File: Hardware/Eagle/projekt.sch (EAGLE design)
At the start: 140 parts, among them IC1 MEGA16-P, IC2 7805T, Q1 BC807-40SMD, Q10 2N2222, Q11 2N2222, Q12 2N2222, Q13 BC807-40SMD, Q14 BC807-40SMD, Q15 BC807-40SMD, Q16 BC807-40SMD, Q17 BC807-40SMD, Q18 BC807-40SMD, Q19 BC807-40SMD, Q2 BC807-40SMD, Q20 2N2222, Q22 2N2222, Q24 2N2222, Q26 2N2222, Q27 2N2222, Q29 2N2222, Q3 BC807-40SMD, Q30 2N2222, Q4 BC807-40SMD, Q5 BC807-40SMD, Q6 2N2222, Q7 2N2222, Q8 2N2222, Q9 2N2222

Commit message: generalne porzadki w kodzie i schemacie
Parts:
- removed LED1, LED2, LED3, LED4, LED5: LA-401AD, led-7-segment:LA-401AD
- added D1, D2, D3, D4, D5: (no value), special:7SEG-CA
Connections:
- net ZASILACZ_1 renamed POWER_1
- net ZASILACZ_2 renamed POWER_2
- removed net N$28: IC1.(TMS)PC3, R1.1
- removed net N$30: IC1.(OC1A)PD5, R14.1
- removed net N$31: IC1.(RXD)PD0, R19.1
- removed net N$32: IC1.(TXD)PD1, R18.1
- removed net N$33: IC1.(INT0)PD2, R17.1
- removed net N$34: IC1.(INT1)PD3, R16.1
- removed net N$35: IC1.(OC1B)PD4, R15.1
- removed net N$37: IC1.(ICP)PD6, R13.1
- removed net N$44: IC1.(OC2)PD7, R5.1
- removed net N$46: IC1.(SCL)PC0, R4.1
- removed net N$47: IC1.(SDA)PC1, R3.1
- removed net N$49: IC1.(TCK)PC2, R2.1
- removed net N$50: IC1.(TDO)PC4, R27.1
- removed net N$64: IC1.(TDI)PC5, R28.1
- removed net N$67: IC1.(TOSC1)PC6, R29.1
- removed net N$68: IC1.(TOSC2)PC7, R30.1
- removed net N$69: IC1.(T0/XCK)PB0, R31.1
- removed net N$7: LED1.G, LED2.G, LED3.G, LED4.G, LED5.G, R12.2
- removed net N$70: IC1.(T1)PB1, R32.1
- removed net N$71: IC1.(ADC0)PA0, R33.1
- removed net N$72: IC1.(ADC1)PA1, R34.1
- removed net N$73: IC1.(ADC2)PA2, R35.1
- removed net N$74: IC1.(ADC3)PA3, R36.1
- removed net N$75: IC1.(ADC4)PA4, R38.1
- removed net N$76: IC1.(ADC5)PA5, R37.1
- removed net N$77: IC1.(ADC6)PA6, R39.1
- removed net N$98: IC1.(ADC7)PA7, R40.1
- new net DISP_ANO_0: IC1.(T0/XCK)PB0, R5.1
- new net DISP_ANO_1: IC1.(T1)PB1, R4.1
- new net DISP_ANO_2: IC1.(AIN0/INT2)PB2, R3.1
- new net DISP_ANO_3: IC1.(AIN1/OC0)PB3, R2.1
- new net DISP_ANO_4: IC1.(SS)PB4, R1.1
- new net DISP_SEG_A: IC1.(ADC0)PA0, R13.1
- new net DISP_SEG_B: IC1.(ADC1)PA1, R14.1
- new net DISP_SEG_C: IC1.(ADC2)PA2, R15.1
- new net DISP_SEG_D: IC1.(ADC3)PA3, R16.1
- new net DISP_SEG_E: IC1.(ADC4)PA4, R17.1
- new net DISP_SEG_F: IC1.(ADC5)PA5, R18.1
- new net DISP_SEG_G: IC1.(ADC6)PA6, R19.1
- new net LED_ANO_1: R40.1
- new net LED_ANO_2: R39.1
- new net LED_ANO_3: R37.1
- new net LED_ANO_4: R38.1
- new net LED_ANO_5: R36.1
- new net LED_ANO_6: R35.1
- new net LED_ANO_7: R34.1
- new net LED_CAT_1: R33.1
- new net LED_CAT_2: R32.1
- new net LED_CAT_3: R31.1
- new net LED_CAT_4: R30.1
- new net LED_CAT_5: R29.1
- new net LED_CAT_6: R28.1
- new net LED_CAT_7: R27.1
- new net N$25: D1.G, D2.G, D3.G, D4.G, D5.G, R12.2
- net KLAW_1: no longer IC1.(SCK)PB7
- net KLAW_2: no longer IC1.(MISO)PB6
- net KLAW_3: no longer IC1.(MOSI)PB5
- net KLAW_4: no longer IC1.(SS)PB4
- net KLAW_5: no longer IC1.(AIN1/OC0)PB3
- net KLAW_6: no longer IC1.(AIN0/INT2)PB2
- net N$1: now also D1.A, D2.A, D3.A, D4.A, D5.A; no longer LED1.A, LED2.A, LED3.A, LED4.A, LED5.A
- net N$10: now also D3.CA1, D3.CA2; no longer LED3.A@1, LED3.A@2
- net N$11: now also D4.CA1, D4.CA2; no longer LED4.A@1, LED4.A@2
- net N$12: now also D5.CA1, D5.CA2; no longer LED5.A@1, LED5.A@2
- net N$2: now also D1.B, D2.B, D3.B, D4.B, D5.B; no longer LED1.B, LED2.B, LED3.B, LED4.B, LED5.B
- net N$3: now also D1.C, D2.C, D3.C, D4.C, D5.C; no longer LED1.C, LED2.C, LED3.C, LED4.C, LED5.C
- net N$4: now also D1.D, D2.D, D3.D, D4.D, D5.D; no longer LED1.D, LED2.D, LED3.D, LED4.D, LED5.D
- net N$5: now also D1.E, D2.E, D3.E, D4.E, D5.E; no longer LED1.E, LED2.E, LED3.E, LED4.E, LED5.E
- net N$6: now also D1.F, D2.F, D3.F, D4.F, D5.F; no longer LED1.F, LED2.F, LED3.F, LED4.F, LED5.F
- net N$8: now also D1.CA1, D1.CA2; no longer LED1.A@1, LED1.A@2
- net N$9: now also D2.CA1, D2.CA2; no longer LED2.A@1, LED2.A@2
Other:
- note added: "330R"
- note added: "47u"
- note added: "7 SEGMENT DISPLAY"
- note added: "KEYBOARD"
- note added: "LED MATRIX"
- note added: "POWER SUPPLY"
- note added: "PROCESSOR"
- note removed: "???"
- note removed: "KLAWIATURA"
- note removed: "ZASILANIE"
- moved on the sheet: B1, C1, C2, C3, C4, C5, C6, C7, IC1, IC2, LED10, LED11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

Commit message: diody i klawiatura
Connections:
- removed net KLAW_1: S1.0@A, S1.0@B, S2.0@A, S2.0@B, S3.0@A, S3.0@B
- removed net KLAW_2: S4.0@A, S4.0@B, S5.0@A, S5.0@B, S6.0@A, S6.0@B
- removed net KLAW_3: S7.0@A, S7.0@B, S8.0@A, S8.0@B, S9.0@A, S9.0@B
- removed net KLAW_4: S3.1@A, S3.1@B, S4.1@A, S4.1@B, S9.1@A, S9.1@B
- removed net KLAW_5: S2.1@A, S2.1@B, S5.1@A, S5.1@B, S8.1@A, S8.1@B
- removed net KLAW_6: S1.1@A, S1.1@B, S6.1@A, S6.1@B, S7.1@A, S7.1@B
- removed net LED_ANO_7: R34.1
- new net KEY_1: IC1.(TOSC2)PC7, S1.0@A, S1.0@B, S2.0@A, S2.0@B, S3.0@A, S3.0@B
- new net KEY_2: IC1.(TOSC1)PC6, S4.0@A, S4.0@B, S5.0@A, S5.0@B, S6.0@A, S6.0@B
- new net KEY_3: IC1.(TDI)PC5, S7.0@A, S7.0@B, S8.0@A, S8.0@B, S9.0@A, S9.0@B
- new net KEY_4: IC1.(TDO)PC4, S3.1@A, S3.1@B, S4.1@A, S4.1@B, S9.1@A, S9.1@B
- new net KEY_5: IC1.(TMS)PC3, S2.1@A, S2.1@B, S5.1@A, S5.1@B, S8.1@A, S8.1@B
- new net KEY_6: IC1.(TCK)PC2, S1.1@A, S1.1@B, S6.1@A, S6.1@B, S7.1@A, S7.1@B
- new net LED_ANO_0: IC1.(ADC7)PA7, R40.1
- net LED_ANO_1: now also IC1.(SCK)PB7, R39.1; no longer R40.1
- net LED_ANO_2: now also IC1.(MISO)PB6, R37.1; no longer R39.1
- net LED_ANO_3: now also IC1.(MOSI)PB5, R38.1; no longer R37.1
- net LED_ANO_4: now also IC1.(SDA)PC1, R36.1; no longer R38.1
- net LED_ANO_5: now also IC1.(SCL)PC0, R35.1; no longer R36.1
- net LED_ANO_6: now also IC1.(OC2)PD7, R34.1; no longer R35.1
- net LED_CAT_1: now also IC1.(RXD)PD0
- net LED_CAT_2: now also IC1.(TXD)PD1
- net LED_CAT_3: now also IC1.(INT0)PD2
- net LED_CAT_4: now also IC1.(INT1)PD3
- net LED_CAT_5: now also IC1.(OC1B)PD4
- net LED_CAT_6: now also IC1.(OC1A)PD5
- net LED_CAT_7: now also IC1.(ICP)PD6

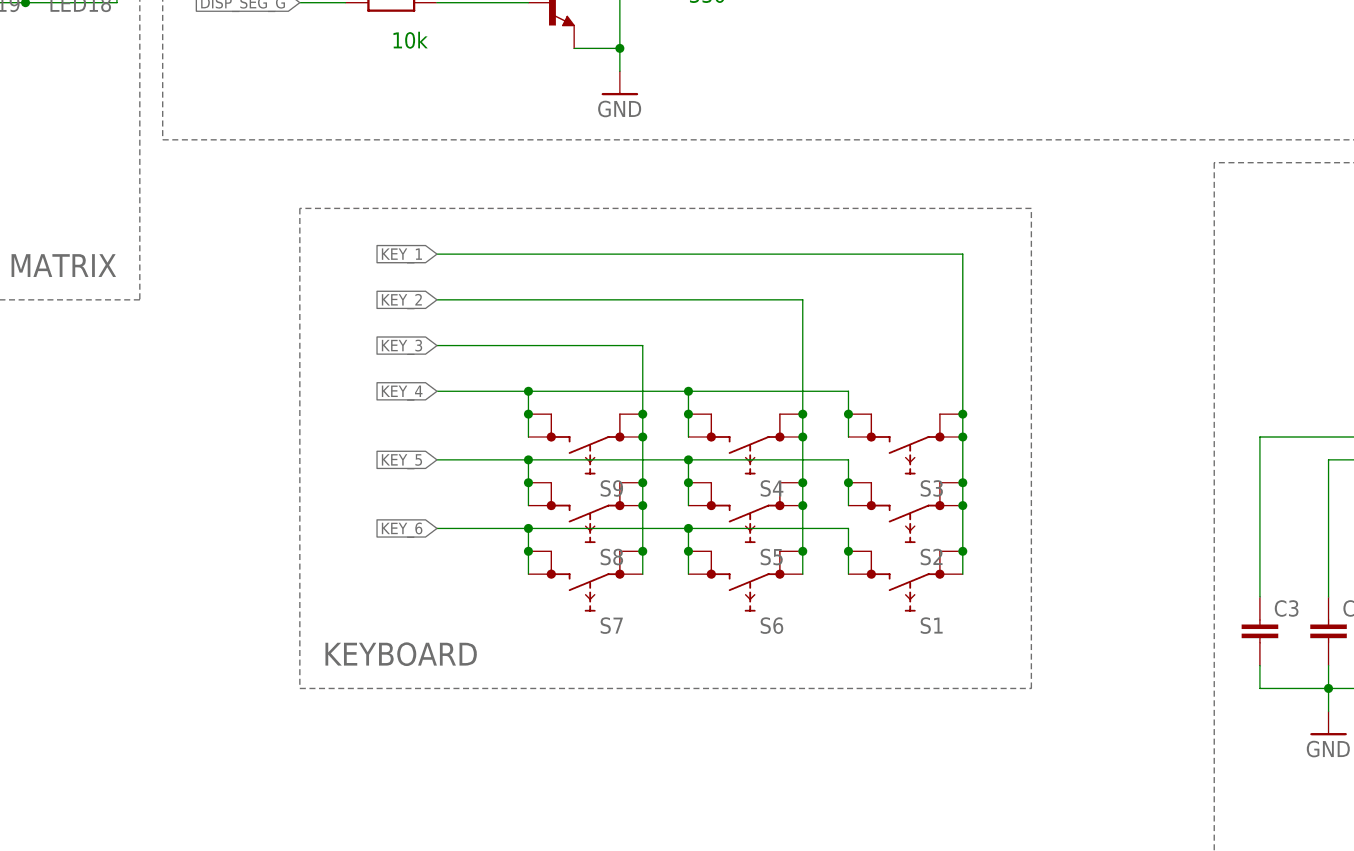
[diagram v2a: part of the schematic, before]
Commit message: multiplekser zamiast klawiatury matrycowej
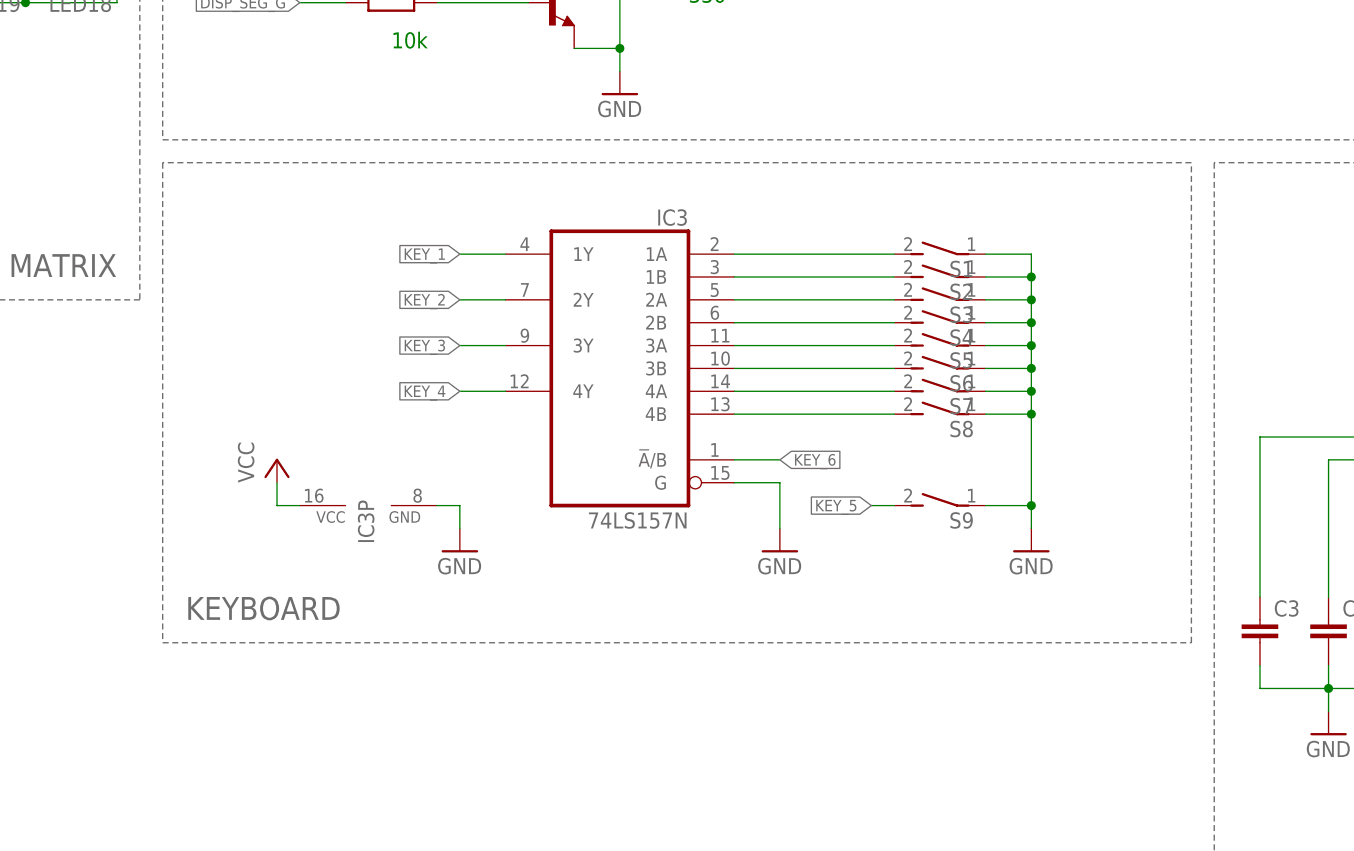
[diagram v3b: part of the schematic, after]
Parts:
- added IC3: 74LS157N, 74xx-eu:74LS157N
- S1, S2, S3, S4, S5, S6, S7, S8, S9: device switch:REKN -> switch-dil:DS01E
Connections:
- new net N$27: IC3A.1B, S2.2
- new net N$28: IC3A.2A, S3.2
- new net N$29: IC3A.2B, S4.2
- new net N$30: IC3A.3A, S5.2
- new net N$31: IC3A.3B, S6.2
- new net N$32: IC3A.4A, S7.2
- new net N$33: IC3A.4B, S8.2
- new net N$7: IC3A.1A, S1.2
- net GND: now also IC3A.G, IC3P.GND, S1.1, S2.1, S3.1, S4.1, S5.1, S6.1, S7.1, S8.1, S9.1
- net KEY_1: now also IC3A.1Y; no longer S1.0@A, S1.0@B, S2.0@A, S2.0@B, S3.0@A, S3.0@B
- net KEY_2: now also IC3A.2Y; no longer S4.0@A, S4.0@B, S5.0@A, S5.0@B, S6.0@A, S6.0@B
- net KEY_3: now also IC3A.3Y; no longer S7.0@A, S7.0@B, S8.0@A, S8.0@B, S9.0@A, S9.0@B
- net KEY_4: now also IC3A.4Y; no longer S3.1@A, S3.1@B, S4.1@A, S4.1@B, S9.1@A, S9.1@B
- net KEY_5: now also S9.2; no longer S2.1@A, S2.1@B, S5.1@A, S5.1@B, S8.1@A, S8.1@B
- net KEY_6: now also IC3A.!A!/B; no longer S1.1@A, S1.1@B, S6.1@A, S6.1@B, S7.1@A, S7.1@B
- net VCC: now also IC3P.VCC

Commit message: przerwania, multiplekser
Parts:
- added R42, R43, R44, R45, R46, R47, R48, R49: (no value), resistor:R-EU_R0805
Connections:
- net N$27: now also R43.1
- net N$28: now also R44.1
- net N$29: now also R45.1
- net N$30: now also R46.1
- net N$31: now also R47.1
- net N$32: now also R48.1
- net N$33: now also R49.1
- net N$7: now also R42.1
- net VCC: now also R42.2, R43.2, R44.2, R45.2, R46.2, R47.2, R48.2, R49.2
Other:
- moved on the sheet: B1, C4, C5, C6, C7, IC2, IC3, IC3P, S1, S2, S3, S4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

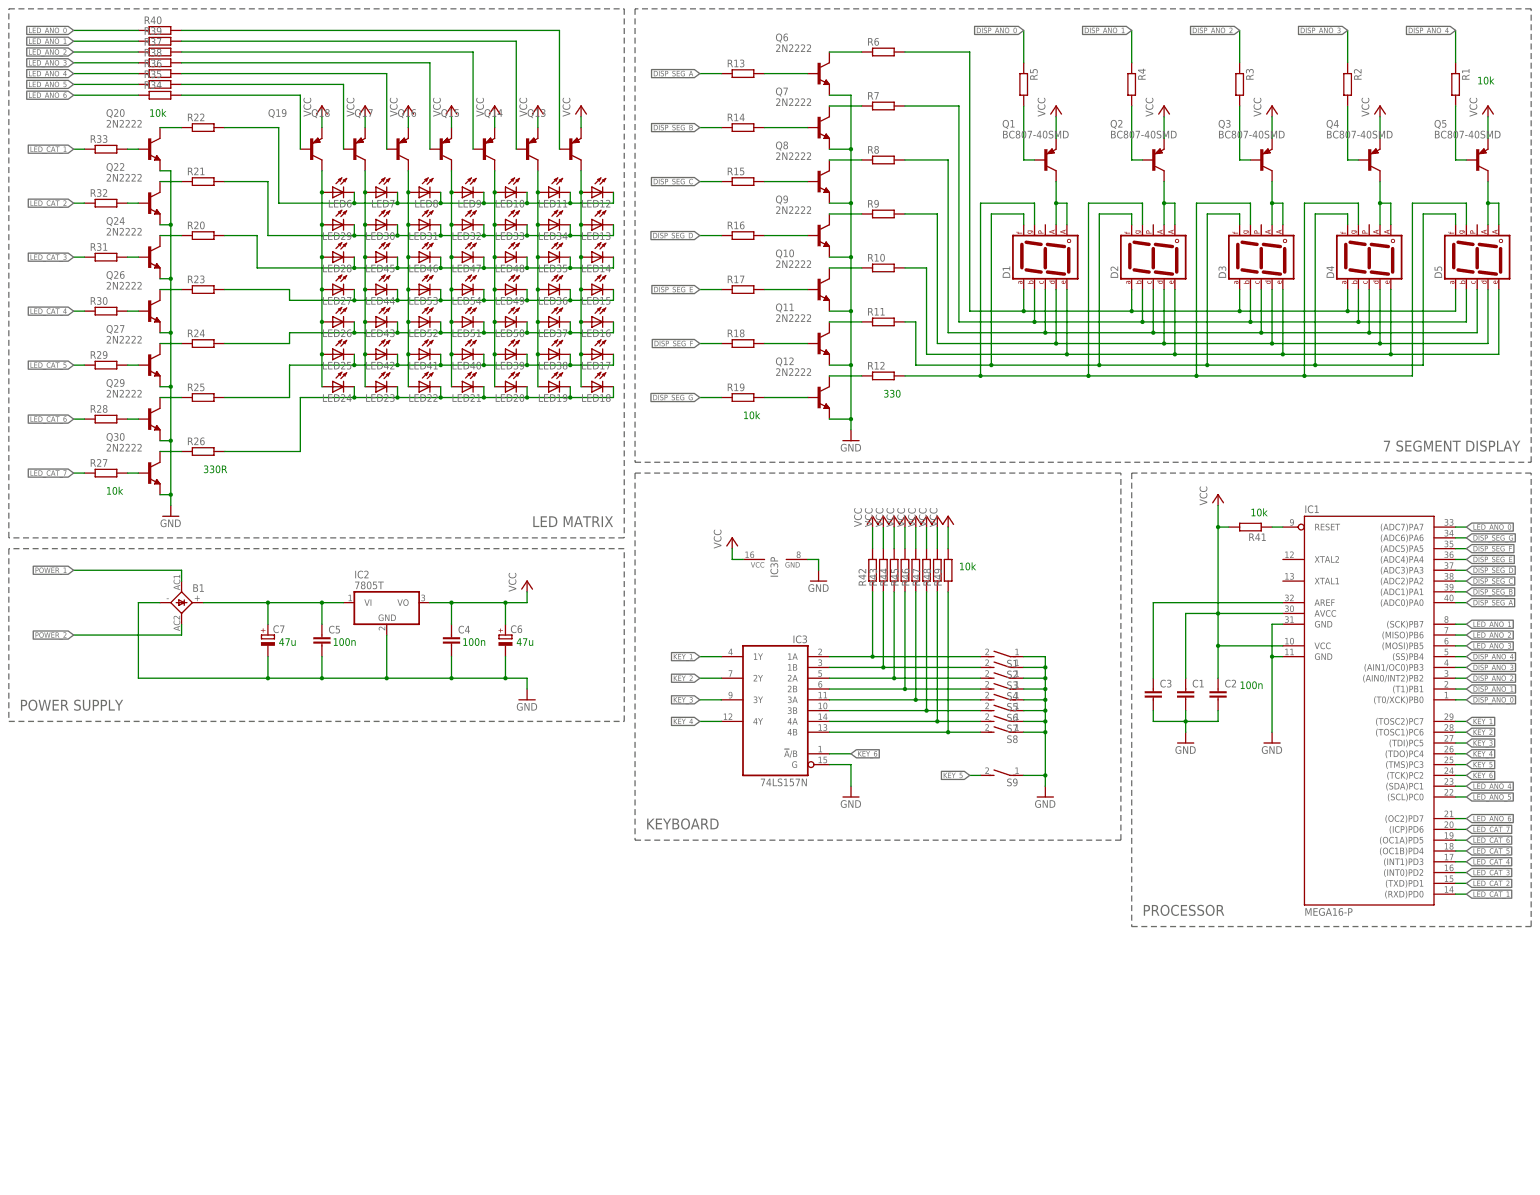
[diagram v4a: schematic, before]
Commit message: wymiana klawiatury
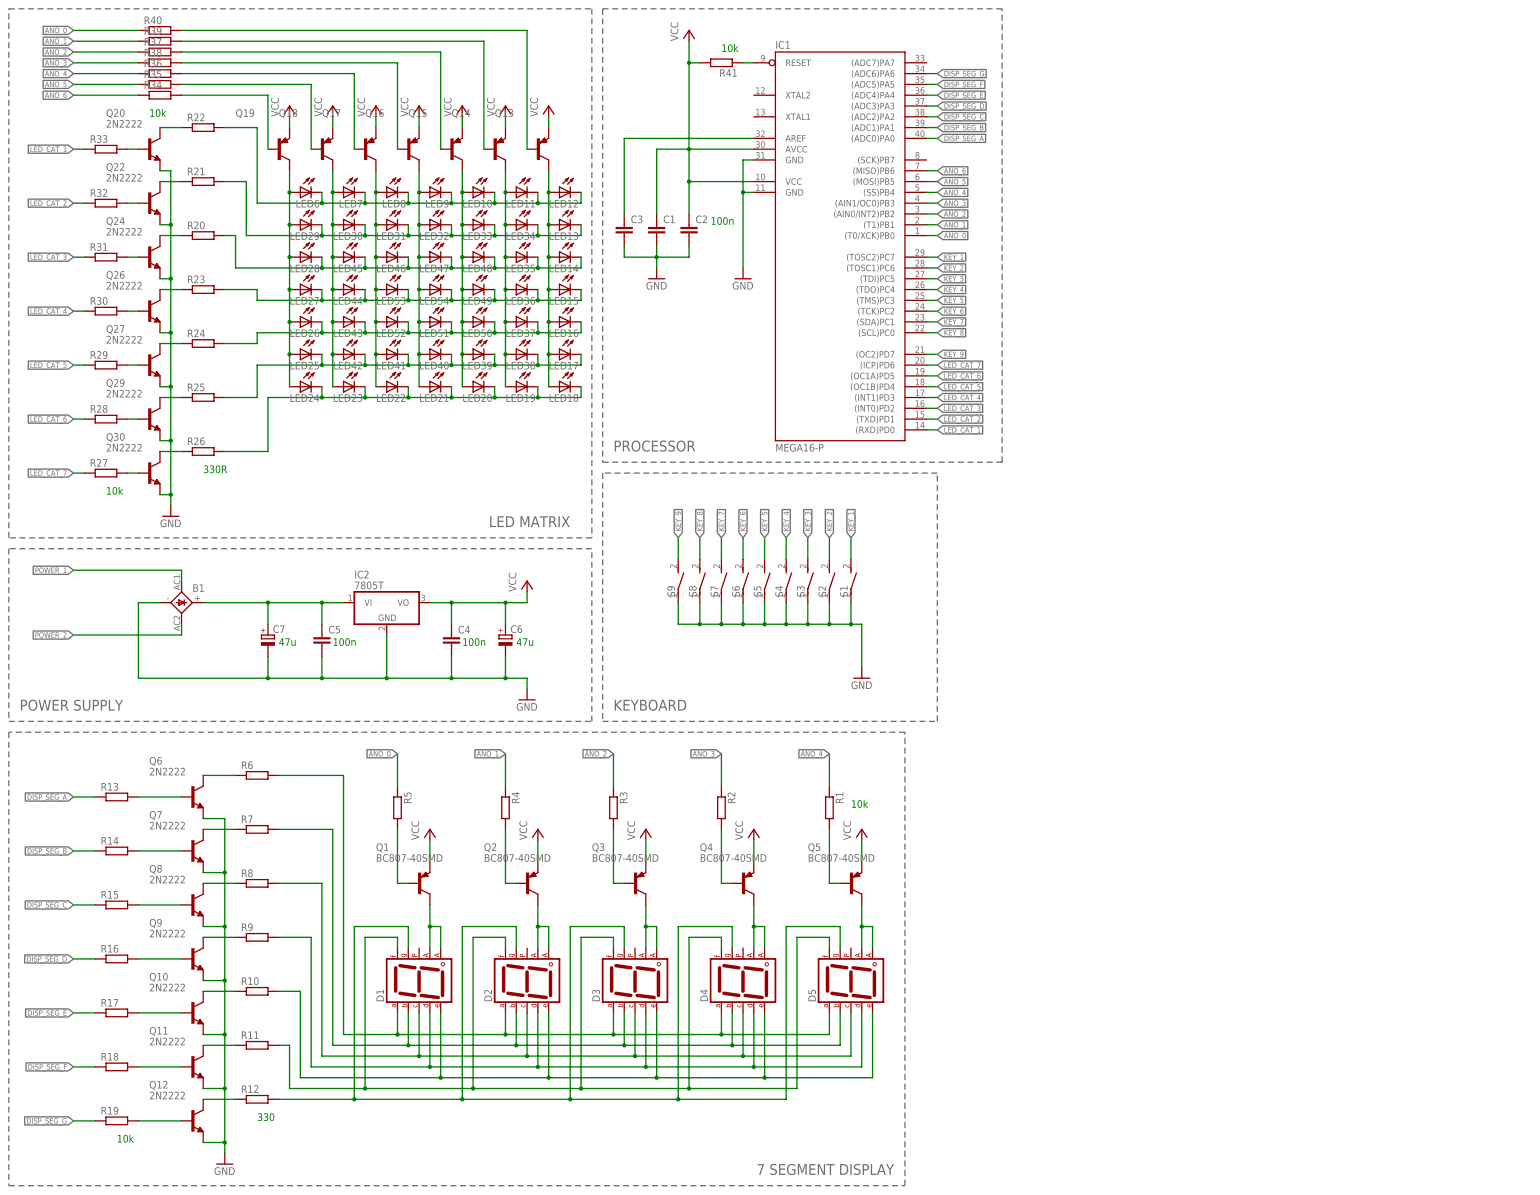
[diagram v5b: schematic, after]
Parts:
- removed IC3: 74LS157N, 74xx-eu:74LS157N
- removed R42, R43, R44, R45, R46, R47, R48, R49: (no value), resistor:R-EU_R0805
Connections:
- removed net DISP_ANO_0: IC1.(T0/XCK)PB0, R5.1
- removed net DISP_ANO_1: IC1.(T1)PB1, R4.1
- removed net DISP_ANO_2: IC1.(AIN0/INT2)PB2, R3.1
- removed net DISP_ANO_3: IC1.(AIN1/OC0)PB3, R2.1
- removed net DISP_ANO_4: IC1.(SS)PB4, R1.1
- removed net LED_ANO_0: IC1.(ADC7)PA7, R40.1
- removed net LED_ANO_1: IC1.(SCK)PB7, R39.1
- removed net LED_ANO_2: IC1.(MISO)PB6, R37.1
- removed net LED_ANO_3: IC1.(MOSI)PB5, R38.1
- removed net LED_ANO_4: IC1.(SDA)PC1, R36.1
- removed net LED_ANO_5: IC1.(SCL)PC0, R35.1
- removed net LED_ANO_6: IC1.(OC2)PD7, R34.1
- removed net N$27: IC3A.1B, R43.1, S2.2
- removed net N$28: IC3A.2A, R44.1, S3.2
- removed net N$29: IC3A.2B, R45.1, S4.2
- removed net N$30: IC3A.3A, R46.1, S5.2
- removed net N$31: IC3A.3B, R47.1, S6.2
- removed net N$32: IC3A.4A, R48.1, S7.2
- removed net N$33: IC3A.4B, R49.1, S8.2
- removed net N$7: IC3A.1A, R42.1, S1.2
- new net ANO_0: IC1.(T0/XCK)PB0, R40.1, R5.1
- new net ANO_1: IC1.(T1)PB1, R39.1, R4.1
- new net ANO_2: IC1.(AIN0/INT2)PB2, R3.1, R37.1
- new net ANO_3: IC1.(AIN1/OC0)PB3, R2.1, R38.1
- new net ANO_4: IC1.(SS)PB4, R1.1, R36.1
- new net ANO_5: IC1.(MOSI)PB5, R35.1
- new net ANO_6: IC1.(MISO)PB6, R34.1
- new net KEY_7: IC1.(SDA)PC1, S7.2
- new net KEY_8: IC1.(SCL)PC0, S8.2
- new net KEY_9: IC1.(OC2)PD7, S9.2
- net GND: no longer IC3A.G, IC3P.GND
- net KEY_1: now also S1.2; no longer IC3A.1Y
- net KEY_2: now also S2.2; no longer IC3A.2Y
- net KEY_3: now also S3.2; no longer IC3A.3Y
- net KEY_4: now also S4.2; no longer IC3A.4Y
- net KEY_5: now also S5.2; no longer S9.2
- net KEY_6: now also S6.2; no longer IC3A.!A!/B
- net VCC: no longer IC3P.VCC, R42.2, R43.2, R44.2, R45.2, R46.2, R47.2, R48.2, R49.2
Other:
- moved on the sheet: C1, C2, C3, D1, D2, D3, D4, D5, IC1, LED10, LED11, LED12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

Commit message: 1.0
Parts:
- LED10, LED11, LED12, LED13, LED14, LED15, LED16, LED17, LED18, LED19, LED20, LED21, LED22, LED23, LED24, LED25, LED26, LED27, LED28, LED29, LED30, LED31, LED32, LED33, LED34, LED35, LED36, LED37, LED38, LED39, LED40, LED41, LED42, LED43, LED44, LED45, LED46, LED47, LED48, LED49, LED50, LED51, LED52, LED53, LED54, LED6, LED7, LED8, LED9: value LEDLUMILED -> (none); device led-lumiled:LEDLUMILED -> led:LED3MM
- Q1, Q13, Q14, Q15, Q16, Q17, Q18, Q19, Q2, Q3, Q4, Q5: value BC807-40SMD -> (none); device transistor-pnp:BC807-40SMD -> transistor:-PNP-TO18-
- R1, R10, R11, R12, R13, R14, R15, R16, R17, R18, R19, R2, R20, R21, R22, R23, R24, R25, R26, R27, R28, R29, R3, R30, R31, R32, R33, R34, R35, R36, R37, R38, R39, R4, R40, R41, R5, R6, R7, R8, R9: device resistor:R-EU_R0805 -> resistor:R-EU_0204/5
